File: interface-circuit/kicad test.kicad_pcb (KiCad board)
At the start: 2 copper layers, 76.2 x 57.2 mm, 17 parts, among them J1 PumpSSR, J2 Probe, J3 GPIO, J4 Buzzer, J5 CoilSwitch, J6 FanPWR, J7 Rpi PWR, J8 PiScreen Power, J9 ATX PWR IN, Q1 2N3904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

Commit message: Debugging board revealed that the transistors on the PCB plan have reversed pin assignments. This commit fixes it.
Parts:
- Q1, Q2, Q3: footprint TO_SOT_Packages_THT:TO-92_Inline_Narrow_Oval -> Custom Components:TO-92_2N3904-Multicomp
- moved Q1 2.54 mm to (165.1, 115.6), turned to 0 degrees
- moved Q2 2.54 mm to (165.1, 128.3), turned to 0 degrees
- moved Q3 2.54 mm to (165.1, 141.0), turned to 0 degrees

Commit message: I found that the Pi could not sink enough power from the USB connection for both itself and the official screen, so I moved the screen's power connecter such that it is now driven directly by the PSU
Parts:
- D1: value UF4004 -> 1N5819
- J8: value PiScreen Power -> ScreenPWR
- moved J8 72.5 mm to (200.7, 130.8), turned to 0 degrees
- moved J6 3.81 mm to (188.0, 138.4)
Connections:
- J3 pad 25: /GND -> (no net)
- J8 pad 1: /5V -> +5V
- J8 pad 2: /GND -> Earth
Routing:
- net /GND: track 31.1 -> 17.3 mm
- net /5V: track 50.8 -> 45.7 mm
- net +5V: track 38.1 -> 43.2 mm
- net +12V: track 61.4 -> 57.6 mm
- net Earth: track 200.5 -> 204.3 mm
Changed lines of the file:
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@@
 (kicad_pcb (version 4) (host pcbnew 4.0.6+dfsg1-1)
   (general
-    (links 33)
+    (links 32)
     (no_connects 0)
-    (area 124.46 97.365 217.4 163.990001)
+    (area 125.654999 98.984999 202.005001 156.285001)
     (thickness 1.6)
     (drawings 6)
-    (tracks 69)
+    (tracks 68)
     (zones 0)
     (modules 17)
@@
       (effects (font (size 1 1) (thickness 0.15)))
     )
-    (fp_text value UF4004 (at 5.08 2.41 270) (layer F.Fab)
+    (fp_text value 1N5819 (at 5.08 2.41 270) (layer F.Fab)
       (effects (font (size 1 1) (thickness 0.15)))
     )
@@
   )
   (module Pin_Headers:Pin_Header_Straight_1x02_Pitch2.54mm (layer F.Cu)
-    (at 191.77 138.43)
+    (at 187.96 138.43)
     (descr "Through hole straight pin header, 1x02, 2.54mm pitch, single row")
     (tags "Through hole pin header THT 1x02 2.54mm single row")
@@
   )
   (module Pin_Headers:Pin_Header_Straight_1x02_Pitch2.54mm (layer F.Cu)
-    (at 128.27 134.62 90)
+    (at 200.66 130.81)
     (descr "Through hole straight pin header, 1x02, 2.54mm pitch, single row")
     (tags "Through hole pin header THT 1x02 2.54mm single row")
-    (fp_text reference J8 (at 0 -2.33 90) (layer F.SilkS)
-      (effects (font (size 1 1) (thickness 0.15)))
-    )
-    (fp_text value "PiScreen Power" (at 0 4.87 90) (layer F.Fab)
+    (fp_text reference J8 (at 0 -2.33) (layer F.SilkS)
+      (effects (font (size 1 1) (thickness 0.15)))
+    )
+    (fp_text value ScreenPWR (at 0 4.87) (layer F.Fab)
       (effects (font (size 1 1) (thickness 0.15)))
     )
@@
     (fp_line (start 1.8 4.35) (end 1.8 -1.8) (layer F.CrtYd) (width 0.05))
     (fp_line (start 1.8 -1.8) (end -1.8 -1.8) (layer F.CrtYd) (width 0.05))
-    (fp_text user %R (at 0 1.27 180) (layer F.Fab)
-      (effects (font (size 1 1) (thickness 0.15)))
-    )
-    (pad 1 thru_hole rect (at 0 0 90) (size 1.7 1.7) (drill 1) (layers *.Cu *.Mask)
-      (net 6 /5V))
-    (pad 2 thru_hole oval (at 0 2.54 90) (size 1.7 1.7) (drill 1) (layers *.Cu *.Mask)
-      (net 4 /GND))
+    (fp_text user %R (at 0 1.27 90) (layer F.Fab)
+      (effects (font (size 1 1) (thickness 0.15)))
+    )
+    (pad 1 thru_hole rect (at 0 0) (size 1.7 1.7) (drill 1) (layers *.Cu *.Mask)
+      (net 12 +5V))
+    (pad 2 thru_hole oval (at 0 2.54) (size 1.7 1.7) (drill 1) (layers *.Cu *.Mask)
+      (net 2 Earth))
     (model ${KISYS3DMOD}/Pin_Headers.3dshapes/Pin_Header_Straight_1x02_Pitch2.54mm.wrl
       (at (xyz 0 0 0))
@@
     (pad 23 thru_hole oval (at 0 27.94) (size 1.7 1.7) (drill 1) (layers *.Cu *.Mask))
     (pad 24 thru_hole oval (at 2.54 27.94) (size 1.7 1.7) (drill 1) (layers *.Cu *.Mask))
-    (pad 25 thru_hole oval (at 0 30.48) (size 1.7 1.7) (drill 1) (layers *.Cu *.Mask)
-      (net 4 /GND))
+    (pad 25 thru_hole oval (at 0 30.48) (size 1.7 1.7) (drill 1) (layers *.Cu *.Mask))
     (pad 26 thru_hole oval (at 2.54 30.48) (size 1.7 1.7) (drill 1) (layers *.Cu *.Mask))
     (pad 27 thru_hole oval (at 0 33.02) (size 1.7 1.7) (drill 1) (layers *.Cu *.Mask))
@@
   (segment (start 176.53 115.57) (end 176.53 138.43) (width 0.25) (layer B.Cu) (net 1))
   (segment (start 176.53 138.43) (end 182.88 138.43) (width 0.25) (layer B.Cu) (net 1))
-  (segment (start 182.88 138.43) (end 191.77 138.43) (width 0.25) (layer B.Cu) (net 1))
+  (segment (start 182.88 138.43) (end 187.96 138.43) (width 0.25) (layer B.Cu) (net 1) (status 20))
+  (segment (start 200.66 133.35) (end 198.12 133.35) (width 0.25) (layer B.Cu) (net 2) (status 400000))
   (segment (start 186.69 119.38) (end 186.69 132.08) (width 0.25) (layer B.Cu) (net 2))
   (segment (start 186.69 104.14) (end 186.69 119.38) (width 0.25) (layer B.Cu) (net 2))
@@
   (segment (start 182.88 148.59) (end 181.69 148.59) (width 0.25) (layer B.Cu) (net 2))
   (segment (start 181.69 148.59) (end 176.53 143.43) (width 0.25) (layer B.Cu) (net 2))
-  (segment (start 191.77 140.97) (end 190.5 140.97) (width 0.25) (layer B.Cu) (net 2))
+  (segment (start 187.96 140.97) (end 190.5 140.97) (width 0.25) (layer B.Cu) (net 2) (status 10))
   (segment (start 190.5 140.97) (end 182.88 148.59) (width 0.25) (layer B.Cu) (net 2))
   (segment (start 165.1 115.57) (end 165.1 119.38) (width 0.25) (layer B.Cu) (net 2))
@@
   (segment (start 133.35 129.54) (end 133.35 119.38) (width 0.25) (layer B.Cu) (net 4))
   (segment (start 133.35 119.38) (end 138.43 114.3) (width 0.25) (layer B.Cu) (net 4))
-  (segment (start 138.43 134.62) (end 130.81 134.62) (width 0.25) (layer B.Cu) (net 4))
-  (segment (start 130.81 134.62) (end 133.35 132.08) (width 0.25) (layer B.Cu) (net 4))
-  (segment (start 133.35 132.08) (end 133.35 129.54) (width 0.25) (layer B.Cu) (net 4))
   (segment (start 130.81 119.38) (end 130.81 129.54) (width 0.25) (layer B.Cu) (net 5))
   (segment (start 130.81 119.38) (end 130.81 115.57) (width 0.25) (layer B.Cu) (net 5))
@@
   (segment (start 140.97 100.33) (end 140.97 104.14) (width 0.25) (layer B.Cu) (net 6))
   (segment (start 128.27 100.33) (end 140.97 100.33) (width 0.25) (layer B.Cu) (net 6))
-  (segment (start 128.27 134.62) (end 128.27 129.54) (width 0.25) (layer B.Cu) (net 6))
   (segment (start 138.43 104.14) (end 130.81 104.14) (width 0.25) (layer B.Cu) (net 7))
   (segment (start 140.97 116.84) (end 146.05 116.84) (width 0.25) (layer B.Cu) (net 8))
@@
   (segment (start 176.49 140.97) (end 176.53 140.93) (width 0.25) (layer B.Cu) (net 11))
   (segment (start 176.49 140.97) (end 176.53 140.93) (width 0.25) (layer B.Cu) (net 11))
+  (segment (start 200.66 130.81) (end 196.85 130.81) (width 0.25) (layer B.Cu) (net 12) (status 400000))
+  (segment (start 196.85 130.81) (end 196.85 129.54) (width 0.25) (layer B.Cu) (net 12))
   (segment (start 191.77 121.92) (end 191.77 129.54) (width 0.25) (layer B.Cu) (net 12))
   (segment (start 196.85 129.54) (end 196.85 104.14) (width 0.25) (layer B.Cu) (net 12))

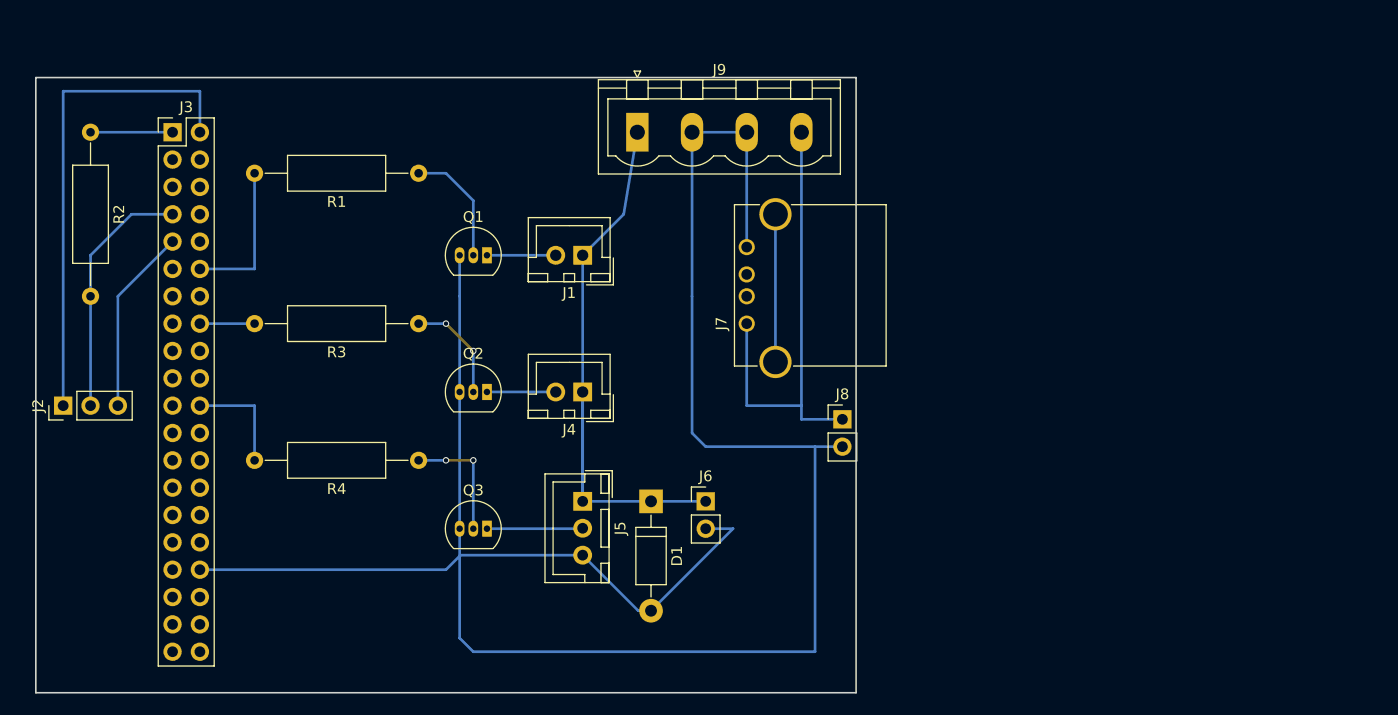
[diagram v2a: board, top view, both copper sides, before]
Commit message: Add transistor control of fan, make pins match 3rd party board, switch to screw terminals
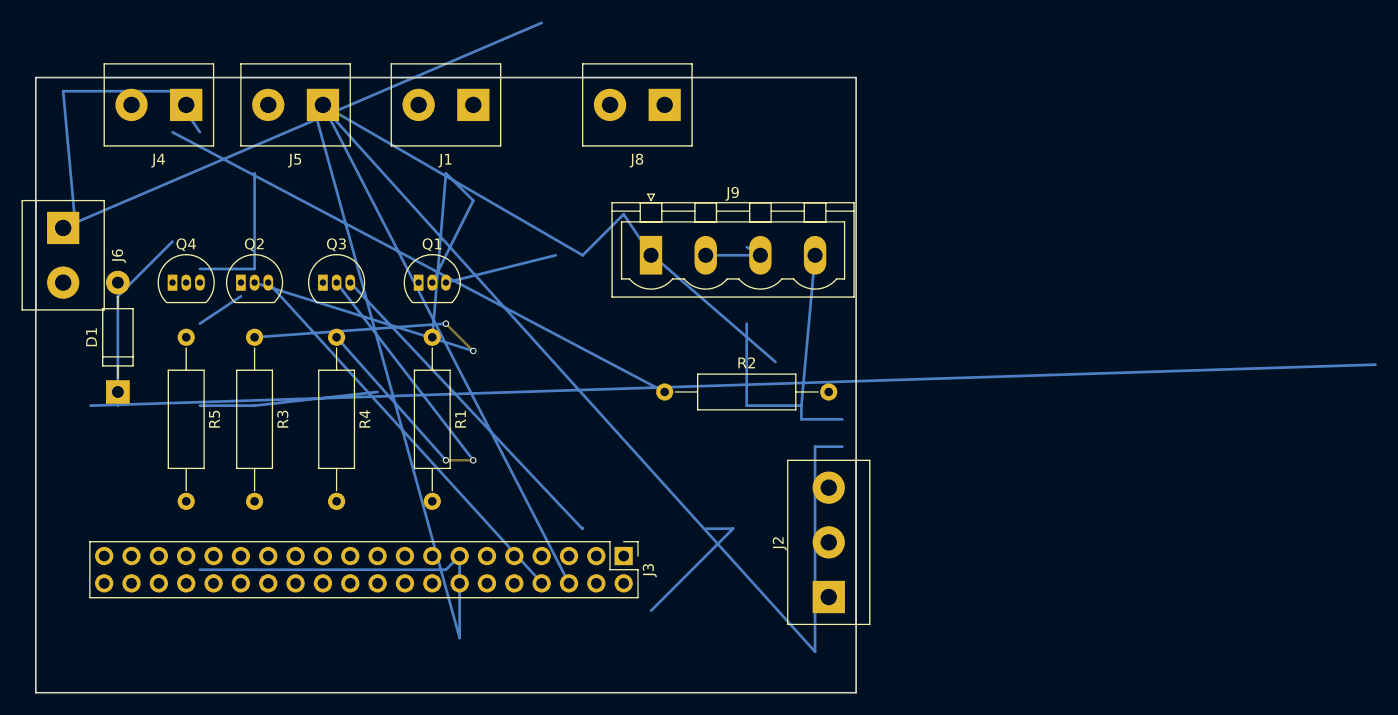
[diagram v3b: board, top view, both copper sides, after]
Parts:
- removed J7: Rpi PWR, Connectors:USB_A
- added Q4: 2N3904, TO_SOT_Packages_THT:TO-92_Inline_Narrow_Oval, F.Cu at (138.4, 118.1)
- added R5: 1R, Resistors_THT:R_Axial_DIN0309_L9.0mm_D3.2mm_P15.24mm_Horizontal, F.Cu at (139.7, 123.2)
- J1, J4: footprint Connectors_JST:JST_XH_B02B-XH-A_02x2.50mm_Straight -> Connectors_Terminal_Blocks:TerminalBlock_bornier-2_P5.08mm
- J2: footprint Pin_Headers:Pin_Header_Straight_1x03_Pitch2.54mm -> Connectors_Terminal_Blocks:TerminalBlock_bornier-3_P5.08mm
- J5: value CoilSwitch -> Coils; footprint Connectors_JST:JST_XH_B03B-XH-A_03x2.50mm_Straight -> Connectors_Terminal_Blocks:TerminalBlock_bornier-2_P5.08mm
- J6, J8: footprint Pin_Headers:Pin_Header_Straight_1x02_Pitch2.54mm -> Connectors_Terminal_Blocks:TerminalBlock_bornier-2_P5.08mm
- Q1, Q2, Q3: footprint Custom Components:TO-92_2N3904-Multicomp -> TO_SOT_Packages_THT:TO-92_Inline_Narrow_Oval
- moved J2 73.3 mm to (199.4, 147.3)
- moved J6 64.9 mm to (128.3, 113.0), turned to 270 degrees
- moved R2 58.5 mm to (184.2, 128.3), turned to 0 degrees
- moved J3 57.5 mm to (180.3, 143.5), turned to 270 degrees
- moved D1 50.6 mm to (133.3, 128.3), turned to 90 degrees
- moved J4 45.5 mm to (139.7, 101.6)
- moved J5 44.0 mm to (152.4, 101.6), turned to 180 degrees
- moved J8 33.6 mm to (184.2, 101.6), turned to 180 degrees
- moved Q3 26.2 mm to (152.4, 118.1)
- moved Q2 22.7 mm to (144.8, 118.1)
- moved J1 17.3 mm to (166.4, 101.6)
- moved R1 15.3 mm to (162.6, 123.2), turned to 270 degrees
- moved R3 15.3 mm to (146.1, 123.2), turned to 270 degrees
- moved R4 13.7 mm to (153.7, 123.2), turned to 270 degrees
- moved J9 11.5 mm to (182.9, 115.6)
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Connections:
- D1 pad 2: Earth -> Net-(D1-Pad2)
- J2 pad 1: /5V -> +5V
- J2 pad 3: /GND -> Earth
- J3 pad 12: Net-(J3-Pad12) -> (no net)
- J3 pad 15: (no net) -> Net-(J3-Pad15)
- J3 pad 16: Net-(J3-Pad16) -> (no net)
- J3 pad 2: /5V -> +5V
- J3 pad 22: Net-(J3-Pad22) -> (no net)
- J3 pad 29: (no net) -> Net-(J3-Pad29)
- J3 pad 31: (no net) -> Net-(J3-Pad31)
- J3 pad 33: (no net) -> Net-(J3-Pad33)
- J3 pad 34: Earth -> (no net)
- J3 pad 39: (no net) -> Earth
- J3 pad 6: (no net) -> Net-(J3-Pad6)
- J3 pad 9: /GND -> Earth
- J5 pad 1: +12V -> Net-(J5-Pad1)
- J5 pad 2: Net-(J5-Pad2) -> Earth
- J6 pad 2: Earth -> Net-(D1-Pad2)
- J8 pad 2: Earth -> Net-(J3-Pad6)
- Q3 pad 1: Net-(J5-Pad2) -> Net-(J5-Pad1)
- R1 pad 2: Net-(J3-Pad12) -> Net-(J3-Pad15)
- R3 pad 2: Net-(J3-Pad16) -> Net-(J3-Pad31)
- R4 pad 2: Net-(J3-Pad22) -> Net-(J3-Pad29)
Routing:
- net Net-(J5-Pad1): track 0.00 -> 254.6 mm
- net (no net): track 0.00 -> 185.2 mm
- net Earth: track 204.3 -> 86.4 mm
- net /5V: track 45.7 -> 0.00 mm
- net +12V: track 57.6 -> 102.2 mm
- net /3v3: track 7.62 -> 51.7 mm
- net Net-(Q2-Pad2): track 9.94 -> 42.7 mm
- net Net-(Q3-Pad2): track 11.4 -> 38.7 mm
- net Net-(J2-Pad2): track 23.2 -> 0.00 mm
- net /GND: track 17.3 -> 0.00 mm
- net Net-(Q1-Pad2): track 11.2 -> 27.4 mm
- net Net-(J3-Pad12): track 14.0 -> 0.00 mm
- net Net-(J7-Pad5): track 13.7 -> 0.00 mm
- net +5V: track 43.2 -> 31.8 mm
- net Net-(J3-Pad22): track 10.2 -> 0.00 mm
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
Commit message: New PCB layout using only screw terminals
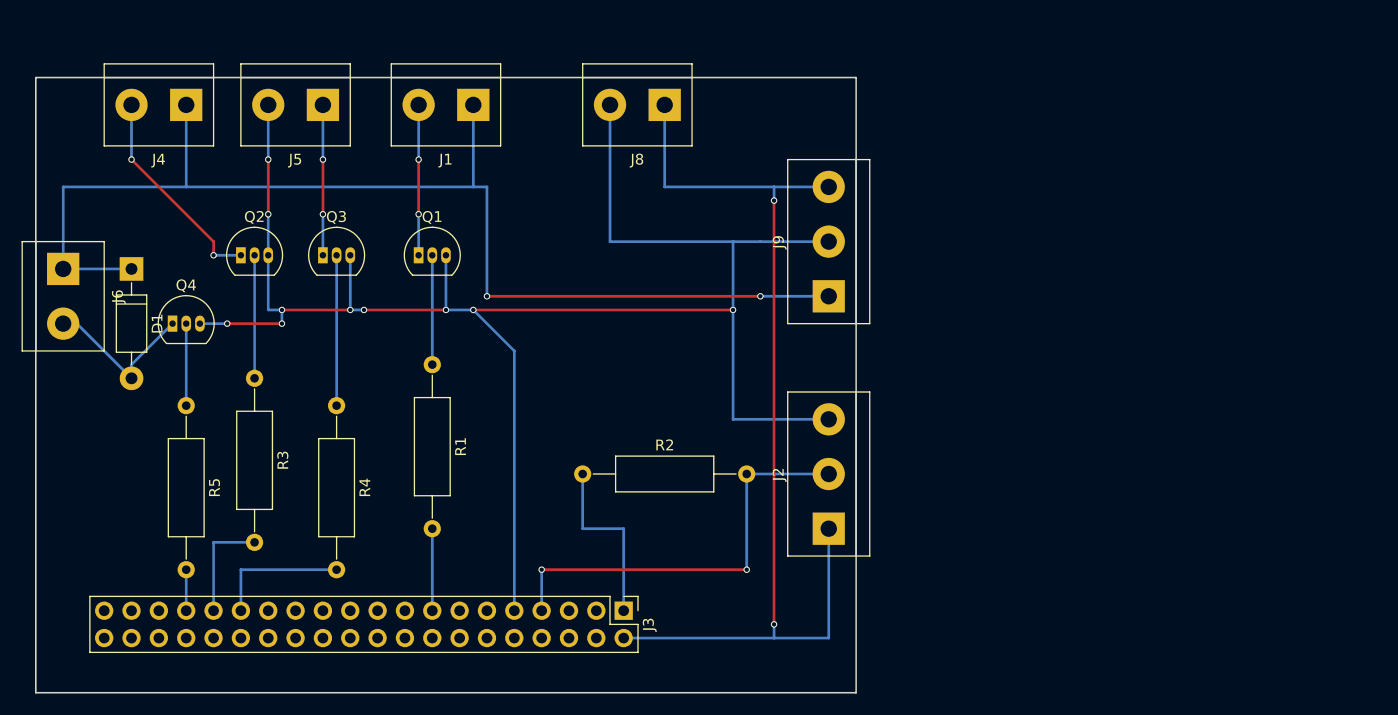
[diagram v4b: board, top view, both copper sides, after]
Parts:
- J9: value ATX PWR IN -> Screw_Terminal_01x03; footprint Connectors_Phoenix:PhoenixContact_MSTBVA-G_04x5.08mm_Vertical -> Connectors_Terminal_Blocks:TerminalBlock_bornier-3_P5.08mm
- moved J9 16.9 mm to (199.4, 119.4), turned to 90 degrees
- moved D1 11.5 mm to (134.6, 116.8), turned to 270 degrees
- moved R2 10.8 mm to (176.5, 135.9)
- moved J2 6.35 mm to (199.4, 141.0)
- moved R4 6.35 mm to (153.7, 129.5)
- moved R5 6.35 mm to (139.7, 129.5)
- moved J3 5.08 mm to (180.3, 148.6)
- moved J6 3.81 mm to (128.3, 116.8)
- moved Q4 3.81 mm to (138.4, 121.9)
- moved R3 3.81 mm to (146.1, 127.0)
- moved Q1 2.54 mm to (161.3, 115.6)
- moved Q2 2.54 mm to (144.8, 115.6)
- moved Q3 2.54 mm to (152.4, 115.6)
- moved R1 2.54 mm to (162.6, 125.7)
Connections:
- J3 pad 39: Earth -> (no net)
- J3 pad 6: Net-(J3-Pad6) -> (no net)
- J8 pad 2: Net-(J3-Pad6) -> Earth
- J9 pad 3: Earth -> +5V
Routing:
- net Net-(J5-Pad1): track 254.6 -> 14.0 mm, vias 0 -> 2
- net (no net): track 185.2 -> 0.00 mm
- net Earth: track 86.4 -> 169.2 mm, vias 0 -> 10
- net +5V: track 31.8 -> 94.0 mm, vias 0 -> 2
- net Net-(J2-Pad2): track 0.00 -> 39.4 mm, vias 0 -> 2
- net /3v3: track 51.7 -> 16.5 mm
- net Net-(Q2-Pad2): track 42.7 -> 11.4 mm, vias 2 -> 0
- net Net-(Q3-Pad2): track 38.7 -> 14.0 mm, vias 2 -> 0
- net Net-(J4-Pad2): track 0.00 -> 19.7 mm, vias 0 -> 2
- net Net-(Q1-Pad2): track 27.4 -> 10.2 mm
- net Net-(D1-Pad2): track 0.00 -> 15.1 mm
- net Net-(J1-Pad2): track 0.00 -> 14.0 mm, vias 0 -> 2
- net Net-(J3-Pad29): track 0.00 -> 12.7 mm
- net Net-(J3-Pad31): track 0.00 -> 10.2 mm
- net +12V: track 102.2 -> 110.5 mm, vias 0 -> 2
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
